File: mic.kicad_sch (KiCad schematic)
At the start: 46 parts, among them J1 AudioPlug3, J2 USB_C_Receptacle_USB2.0_16P, SW1 SW_Push, U1 TS5A3159ADBVR, U2 INA826AID, U3 PCM2902CDBR, U4 TLV70033_SOT23-5, U5 USBLC6-2SC6, Y1 12MHz

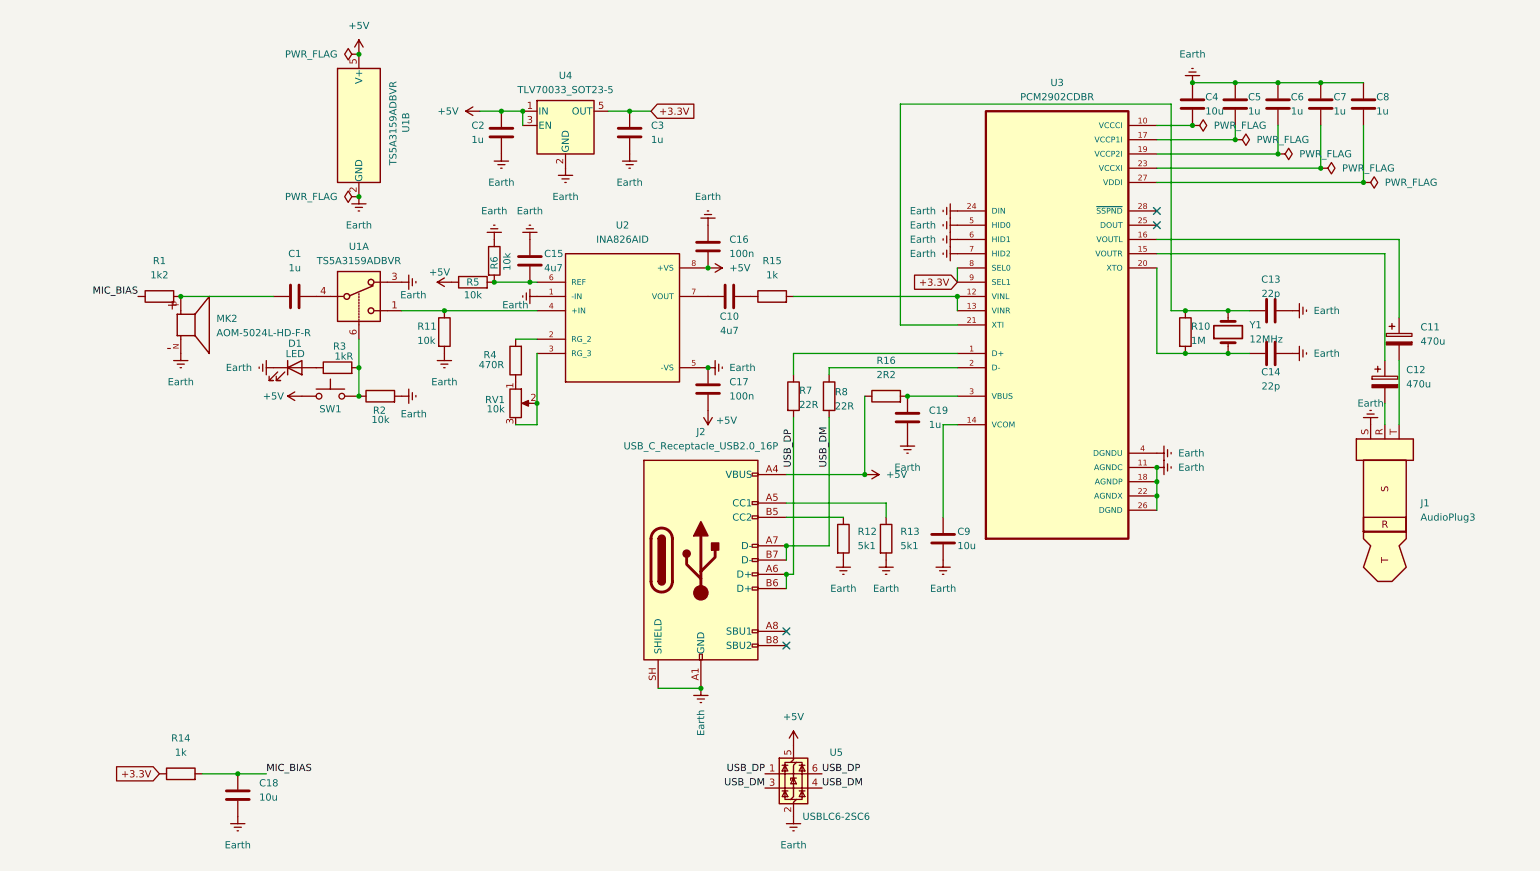
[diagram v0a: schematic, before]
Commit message: needs via, otherwise should be done)
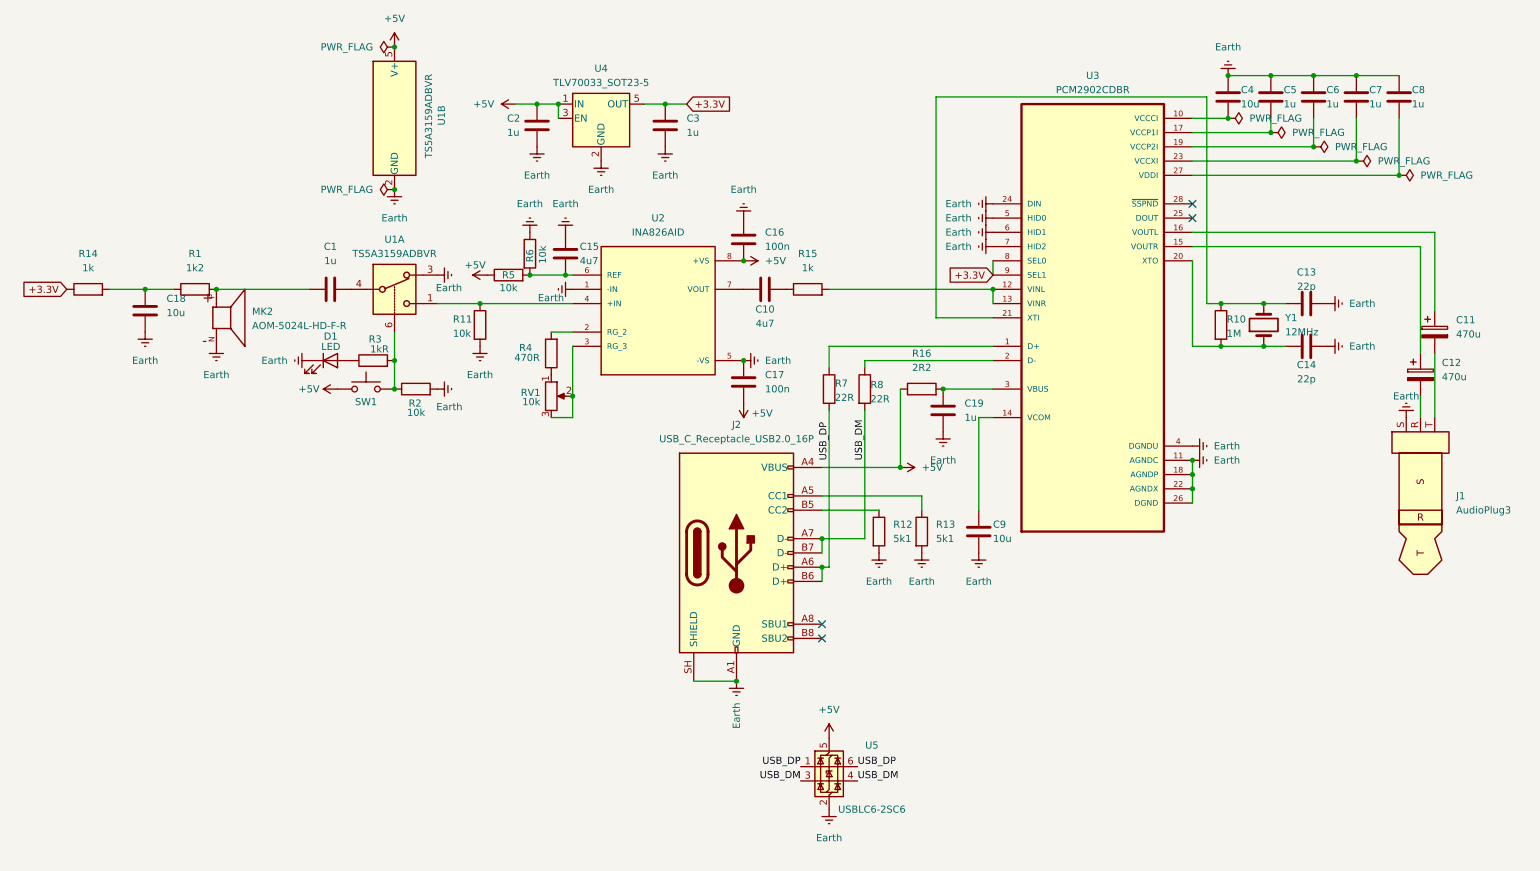
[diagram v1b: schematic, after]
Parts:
- U4: LCSC C11337 -> (none)
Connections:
- net MIC_BIAS: no longer names the net of C18.1, R1.1, R14.2
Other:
- moved on the sheet: C1, C10, C11, C12, C13, C14, C15, C16, C17, C18, C19, C2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

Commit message: final tht
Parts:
- added C21: 100n, Capacitor_THT:C_Disc_D3.4mm_W2.1mm_P2.50mm, symbol Device:C
- added C22: 1u, Capacitor_THT:C_Disc_D3.4mm_W2.1mm_P2.50mm, symbol Device:C
- added R18: 100k, Resistor_THT:R_Axial_DIN0204_L3.6mm_D1.6mm_P2.54mm_Vertical, symbol Device:R
- added U6: 74LVC1G74DP, Package_SO:TSSOP-8_3x3mm_P0.65mm, symbol 74xGxx:74AUC1G74
- R2: value 10k -> 100k
- RV1: LCSC C97444 -> C470577
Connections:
- net +5V: now also R18.1, U6.7 (~{PRE}), U6.8 (VCC)
- net Earth: now also C21.2, C22.2, U6.4 (GND)
- net at R2.1, SW1.2: now also C21.1, U6.1 (C); no longer R3.2, U1.6
- new net: R3.2, U1.6, U6.2 (D), U6.3 (~{Q})
- new net: C22.1, R18.2, U6.6 (~{CLR})
- no-connect marks 4 -> 5
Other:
- moved on the sheet: R2

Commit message: smd version, took only few hours
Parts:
- added C20: 100n, Capacitor_SMD:C_0603_1608Metric, symbol Device:C
- added R9: 1k5R, Resistor_SMD:R_0603_1608Metric, symbol Device:R
- C1, C19, C2, C22, C3, C5, C6, C7, C8: footprint Capacitor_THT:C_Disc_D3.4mm_W2.1mm_P2.50mm -> Capacitor_SMD:C_0603_1608Metric; LCSC C1620326 -> C15849
- C10, C15: footprint Capacitor_THT:C_Disc_D3.4mm_W2.1mm_P2.50mm -> Capacitor_SMD:C_0603_1608Metric; LCSC (none) -> C19666
- C11, C12: footprint Capacitor_THT:CP_Radial_D8.0mm_P3.50mm -> Capacitor_SMD:CP_Elec_8x10; LCSC C1579341 -> C2858857
- C13, C14: footprint Capacitor_THT:C_Disc_D3.4mm_W2.1mm_P2.50mm -> Capacitor_SMD:C_0603_1608Metric; LCSC C2170230 -> C1653
- C16, C17, C21: footprint Capacitor_THT:C_Disc_D3.4mm_W2.1mm_P2.50mm -> Capacitor_SMD:C_0603_1608Metric; LCSC C1620210 -> C149620
- C18, C4, C9: footprint Capacitor_THT:C_Disc_D3.4mm_W2.1mm_P2.50mm -> Capacitor_SMD:C_0603_1608Metric; LCSC C1620730 -> C19702
- D1: LCSC (none) -> C2917798
- J2: footprint Connector_USB:USB_C_Receptacle_G-Switch_GT-USB-7051x -> mic:USB_C_Receptacle_G-Switch_GT-USB-7051x_NoA8
- MK2: footprint AOM-5024L-HD-F-R:MIC_AOM-5024L-HD-F-R -> mic:MIC_AOM-5024L-HD-F-R; LCSC (none) -> C3273730
- R1: footprint Resistor_THT:R_Axial_DIN0204_L3.6mm_D1.6mm_P2.54mm_Vertical -> Resistor_SMD:R_0603_1608Metric; LCSC (none) -> C22765
- R10: footprint Resistor_THT:R_Axial_DIN0204_L3.6mm_D1.6mm_P2.54mm_Vertical -> Resistor_SMD:R_0603_1608Metric; LCSC (none) -> C22935
- R11, R5, R6: footprint Resistor_THT:R_Axial_DIN0204_L3.6mm_D1.6mm_P2.54mm_Vertical -> Resistor_SMD:R_0603_1608Metric; LCSC (none) -> C98220
- R12, R13: footprint Resistor_THT:R_Axial_DIN0204_L3.6mm_D1.6mm_P2.54mm_Vertical -> Resistor_SMD:R_0603_1608Metric; LCSC (none) -> C23186
- R14, R15, R3: footprint Resistor_THT:R_Axial_DIN0204_L3.6mm_D1.6mm_P2.54mm_Vertical -> Resistor_SMD:R_0603_1608Metric; LCSC (none) -> C22548
- R16: footprint Resistor_THT:R_Axial_DIN0204_L3.6mm_D1.6mm_P2.54mm_Vertical -> Resistor_SMD:R_0603_1608Metric; LCSC (none) -> C112307
- R18, R2: footprint Resistor_THT:R_Axial_DIN0204_L3.6mm_D1.6mm_P2.54mm_Vertical -> Resistor_SMD:R_0603_1608Metric; LCSC (none) -> C25803
- R4: footprint Resistor_THT:R_Axial_DIN0204_L3.6mm_D1.6mm_P2.54mm_Vertical -> Resistor_SMD:R_0603_1608Metric; LCSC (none) -> C23179
- R7, R8: footprint Resistor_THT:R_Axial_DIN0204_L3.6mm_D1.6mm_P2.54mm_Vertical -> Resistor_SMD:R_0603_1608Metric; LCSC (none) -> C23345
- U2: footprint INA826AID:SOIC127P599X175-8N -> mic:SOIC127P599X175-8N
- U3: footprint PCM2902C:SOP65P780X200-28N -> mic:SOP65P780X200-28N; LCSC (none) -> C2651869
- U4: LCSC (none) -> C11337
- Y1: footprint Crystal:Crystal_C26-LF_D2.1mm_L6.5mm_Vertical -> Crystal:Crystal_SMD_5032-2Pin_5.0x3.2mm; LCSC C326537 -> C112573
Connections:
- net +5V: now also C20.1
- net Earth: now also C20.2
- net at R7.1, U3.1 (D+): now also R9.1
- net at C8.2, U3.27 (VDDI): now also R9.2

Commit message: fixed errors
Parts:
- added C23: 100n, Capacitor_SMD:C_0603_1608Metric, symbol Device:C
- added U7: SN74LVC1G17DBVR, Package_TO_SOT_SMD:SOT-23-5, symbol 74xGxx:74LVC1G17
- R1: value 1k2 -> 2k2; LCSC C22765 -> C4190
- R14: value 1k -> 470R; LCSC C22548 -> C23179
- SW1: LCSC C285524 -> alr C51018255
- U6: LCSC C458768 -> C548409
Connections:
- net +5V: now also C23.1, U7.5 (VCC)
- net Earth: now also C23.2, U7.3 (GND)
- net USB_DM: no longer J2.A7 (D-), J2.B7 (D-), U5.3 (I/O2)
- net USB_DP: no longer J2.A6 (D+), J2.B6 (D+), U5.1 (I/O1)
- net BTN_RC: now reaches C21.1, R2.1, SW1.2
- net BTN_RC: now also U7.2; no longer U6.1 (C)
- new net BTN_CLK: U6.1 (C), U7.4
- new net _USB_DM: J2.A7 (D-), J2.B7 (D-), U5.3 (I/O2)
- new net _USB_DP: J2.A6 (D+), J2.B6 (D+), U5.1 (I/O1)
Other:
- moved on the sheet: R2, U5
